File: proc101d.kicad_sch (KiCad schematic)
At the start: 0 parts

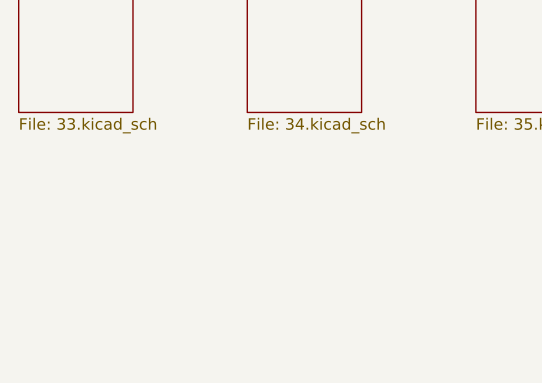
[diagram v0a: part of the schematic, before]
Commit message: fix 1. add mounting holes, remove rule areas around. 2. change net class clearance and minimal via size.
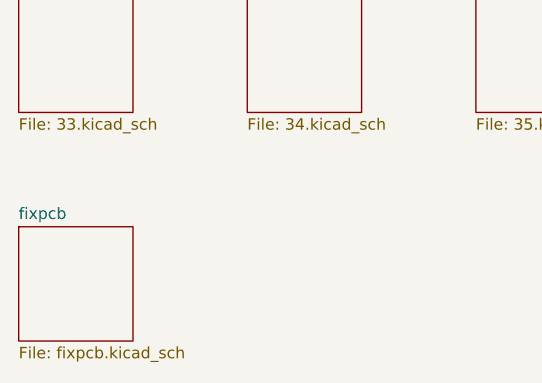
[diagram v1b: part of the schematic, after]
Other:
- added sheet fixpcb (fixpcb.kicad_sch)
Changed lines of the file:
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@@
+	)
+	(sheet
+		(at 38.1 165.1)
+		(size 12.7 12.7)
+		(fields_autoplaced yes)
+		(stroke
+			(width 0.1524)
+			(type solid)
+		)
+		(fill
+			(color 0 0 0 0.0000)
+		)
+		(property "Sheetname" "fixpcb"
+			(at 38.1 164.3884 0)
+			(effects
+				(font
+					(size 1.27 1.27)
+				)
+				(justify left bottom)
+			)
+		)
+		(property "Sheetfile" "fixpcb.kicad_sch"
+			(at 38.1 178.3846 0)
+			(effects
+				(font
+					(size 1.27 1.27)
+				)
+				(justify left top)
+			)
+		)
+		(instances
+			(project "proc101d"
+				(path "/d798ab61-bfb1-4e3e-a919-55e6a99857b1"
+					(page "35")
+				)
+			)
+		)
 	)
 	(sheet

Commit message: a lot, mpu power almost ready.
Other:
- removed sheet 01
- removed sheet ft4232
- removed sheet icssg_rgmii_1_phy
- removed sheet icssg_rgmii_2_phy
- removed sheet mechanical
- removed sheet mipi
- removed sheet test_auto
- removed sheet xds110
- added sheet usb-power-efuse (usb-power-efuse.kicad_sch)
